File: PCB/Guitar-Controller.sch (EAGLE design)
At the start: 33 parts

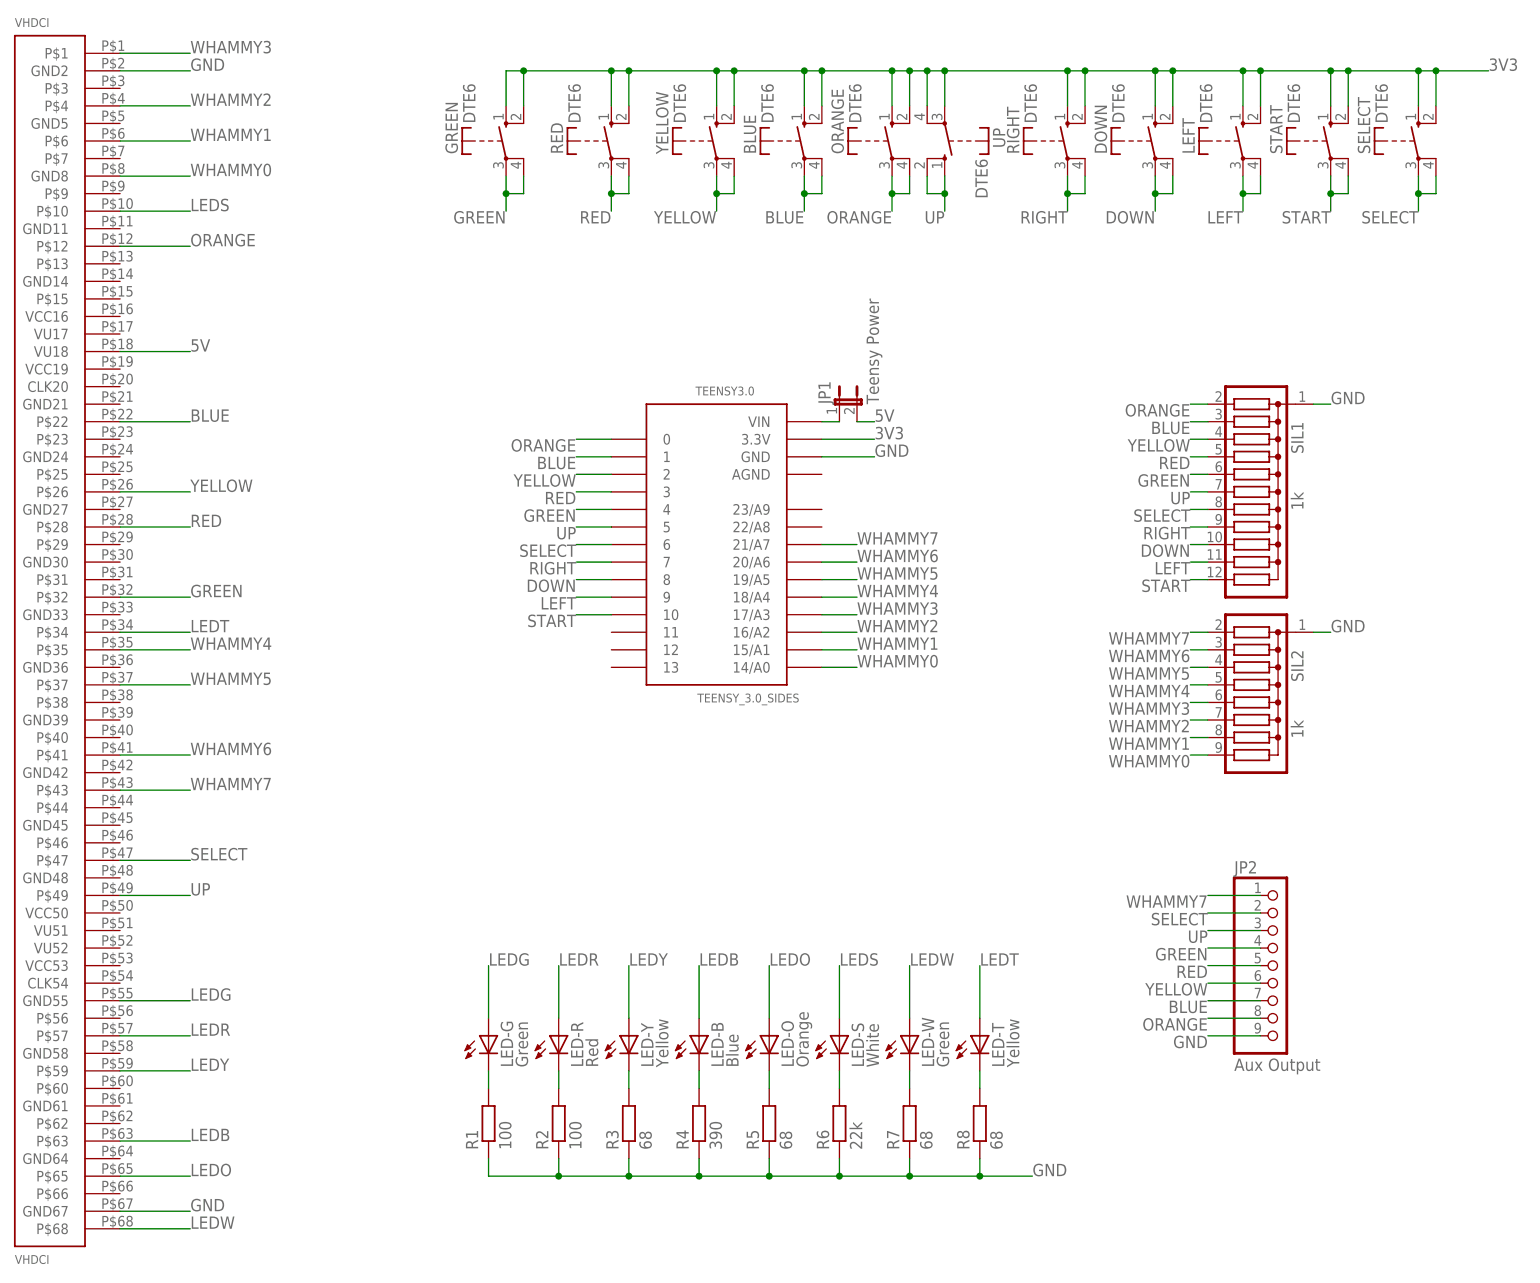
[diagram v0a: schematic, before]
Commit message: PCB: Changed all pin connections to use bottom layer
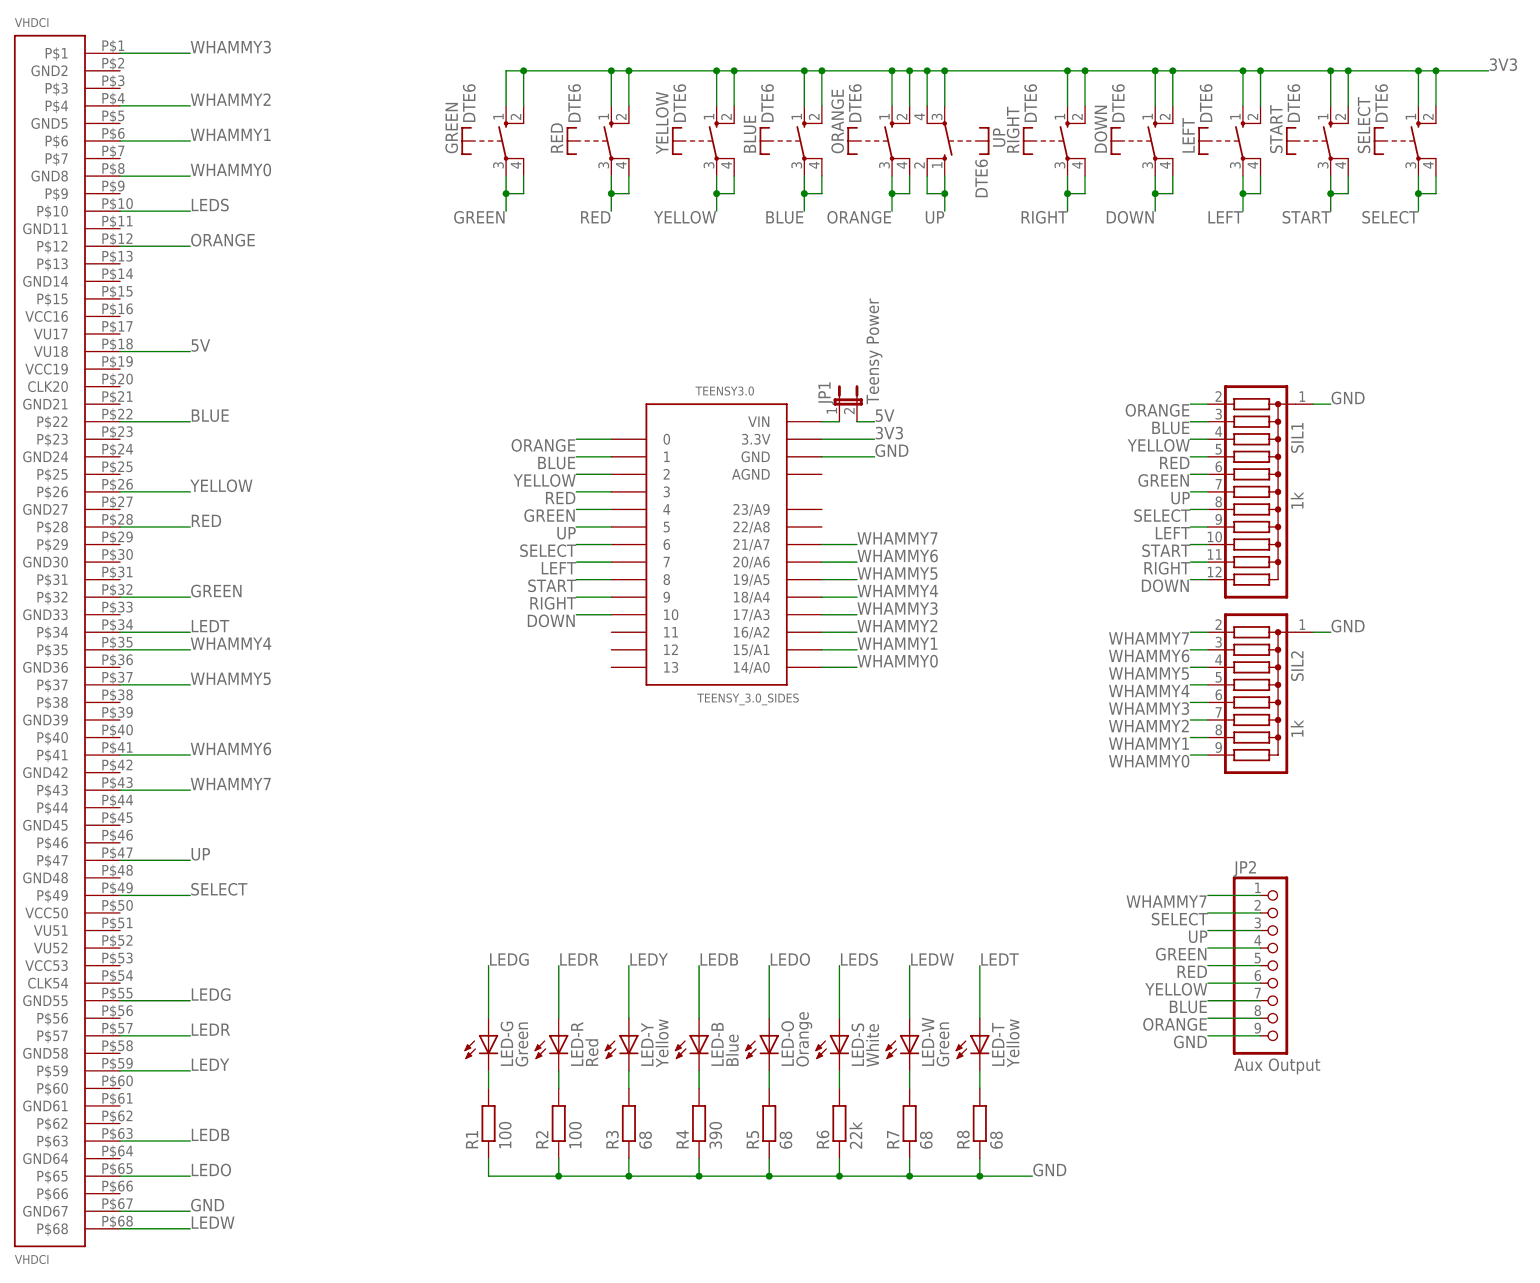
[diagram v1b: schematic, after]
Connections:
- net DOWN: now also SIL1.12, TEENSY3.0.10; no longer SIL1.10, TEENSY3.0.8
- net GND: no longer VHDCI.GND2
- net LEFT: now also SIL1.9, TEENSY3.0.7; no longer SIL1.11, TEENSY3.0.9
- net RIGHT: now also SIL1.11, TEENSY3.0.9; no longer SIL1.9, TEENSY3.0.7
- net SELECT: now also VHDCI.P$49; no longer VHDCI.P$47
- net START: now also SIL1.10, TEENSY3.0.8; no longer SIL1.12, TEENSY3.0.10
- net UP: now also VHDCI.P$47; no longer VHDCI.P$49
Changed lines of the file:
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@@
-</segment>
-<segment>
-<pinref part="VHDCI" gate="G$1" pin="GND2"/>
-<wire x1="-40.64" y1="127" x2="-30.48" y2="127" width="0.1524" layer="91"/>
-<label x="-30.48" y="127" size="1.778" layer="95"/>
 </segment>
 <segment>
@@
 </segment>
 <segment>
-<pinref part="VHDCI" gate="G$1" pin="P$49"/>
-<wire x1="-30.48" y1="7.62" x2="-40.64" y2="7.62" width="0.1524" layer="91"/>
-<label x="-30.48" y="7.62" size="1.778" layer="95"/>
+<pinref part="VHDCI" gate="G$1" pin="P$47"/>
+<wire x1="-30.48" y1="12.7" x2="-40.64" y2="12.7" width="0.1524" layer="91"/>
+<label x="-30.48" y="12.7" size="1.778" layer="95"/>
 </segment>
 </net>
@@
 </segment>
 <segment>
-<pinref part="SIL1" gate="A" pin="10"/>
-<wire x1="116.84" y1="58.42" x2="114.3" y2="58.42" width="0.1524" layer="91"/>
-<label x="114.3" y="58.42" size="1.778" layer="95" rot="R180"/>
-</segment>
-<segment>
-<pinref part="TEENSY3.0" gate="G$1" pin="8"/>
-<wire x1="30.48" y1="53.34" x2="25.4" y2="53.34" width="0.1524" layer="91"/>
-<label x="25.4" y="53.34" size="1.778" layer="95" rot="R180"/>
+<pinref part="TEENSY3.0" gate="G$1" pin="10"/>
+<wire x1="30.48" y1="48.26" x2="25.4" y2="48.26" width="0.1524" layer="91"/>
+<label x="25.4" y="48.26" size="1.778" layer="95" rot="R180"/>
+</segment>
+<segment>
+<pinref part="SIL1" gate="A" pin="12"/>
+<wire x1="116.84" y1="53.34" x2="114.3" y2="53.34" width="0.1524" layer="91"/>
+<label x="114.3" y="53.34" size="1.778" layer="95" rot="R180"/>
 </segment>
 </net>
@@
 </segment>
 <segment>
-<pinref part="SIL1" gate="A" pin="11"/>
-<wire x1="116.84" y1="55.88" x2="114.3" y2="55.88" width="0.1524" layer="91"/>
-<label x="114.3" y="55.88" size="1.778" layer="95" rot="R180"/>
-</segment>
-<segment>
-<pinref part="TEENSY3.0" gate="G$1" pin="9"/>
-<wire x1="30.48" y1="50.8" x2="25.4" y2="50.8" width="0.1524" layer="91"/>
-<label x="25.4" y="50.8" size="1.778" layer="95" rot="R180"/>
+<pinref part="TEENSY3.0" gate="G$1" pin="7"/>
+<wire x1="30.48" y1="55.88" x2="25.4" y2="55.88" width="0.1524" layer="91"/>
+<label x="25.4" y="55.88" size="1.778" layer="95" rot="R180"/>
+</segment>
+<segment>
+<pinref part="SIL1" gate="A" pin="9"/>
+<wire x1="116.84" y1="60.96" x2="114.3" y2="60.96" width="0.1524" layer="91"/>
+<label x="114.3" y="60.96" size="1.778" layer="95" rot="R180"/>
 </segment>
 </net>
@@
 </segment>
 <segment>
-<pinref part="SIL1" gate="A" pin="9"/>
-<wire x1="116.84" y1="60.96" x2="114.3" y2="60.96" width="0.1524" layer="91"/>
-<label x="114.3" y="60.96" size="1.778" layer="95" rot="R180"/>
-</segment>
-<segment>
-<pinref part="TEENSY3.0" gate="G$1" pin="7"/>
-<wire x1="30.48" y1="55.88" x2="25.4" y2="55.88" width="0.1524" layer="91"/>
-<label x="25.4" y="55.88" size="1.778" layer="95" rot="R180"/>
+<pinref part="TEENSY3.0" gate="G$1" pin="9"/>
+<wire x1="30.48" y1="50.8" x2="25.4" y2="50.8" width="0.1524" layer="91"/>
+<label x="25.4" y="50.8" size="1.778" layer="95" rot="R180"/>
+</segment>
+<segment>
+<pinref part="SIL1" gate="A" pin="11"/>
+<wire x1="116.84" y1="55.88" x2="114.3" y2="55.88" width="0.1524" layer="91"/>
+<label x="114.3" y="55.88" size="1.778" layer="95" rot="R180"/>
 </segment>
 </net>
@@
 </segment>
 <segment>
-<pinref part="SIL1" gate="A" pin="12"/>
-<wire x1="116.84" y1="53.34" x2="114.3" y2="53.34" width="0.1524" layer="91"/>
-<label x="114.3" y="53.34" size="1.778" layer="95" rot="R180"/>
-</segment>
-<segment>
-<pinref part="TEENSY3.0" gate="G$1" pin="10"/>
-<wire x1="30.48" y1="48.26" x2="25.4" y2="48.26" width="0.1524" layer="91"/>
-<label x="25.4" y="48.26" size="1.778" layer="95" rot="R180"/>
+<pinref part="TEENSY3.0" gate="G$1" pin="8"/>
+<wire x1="30.48" y1="53.34" x2="25.4" y2="53.34" width="0.1524" layer="91"/>
+<label x="25.4" y="53.34" size="1.778" layer="95" rot="R180"/>
+</segment>
+<segment>
+<pinref part="SIL1" gate="A" pin="10"/>
+<wire x1="116.84" y1="58.42" x2="114.3" y2="58.42" width="0.1524" layer="91"/>
+<label x="114.3" y="58.42" size="1.778" layer="95" rot="R180"/>
 </segment>
 </net>
@@
 </segment>
 <segment>
-<pinref part="VHDCI" gate="G$1" pin="P$47"/>
-<wire x1="-30.48" y1="12.7" x2="-40.64" y2="12.7" width="0.1524" layer="91"/>
-<label x="-30.48" y="12.7" size="1.778" layer="95"/>
-</segment>
-</net>
+<pinref part="VHDCI" gate="G$1" pin="P$49"/>
+<wire x1="-30.48" y1="7.62" x2="-40.64" y2="7.62" width="0.1524" layer="91"/>
+<label x="-30.48" y="7.62" size="1.778" layer="95"/>
+</segment>
+</net>

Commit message: PCB: Fixed errors on VHDC connector and changed SILs SIL change is to work with what is available in department
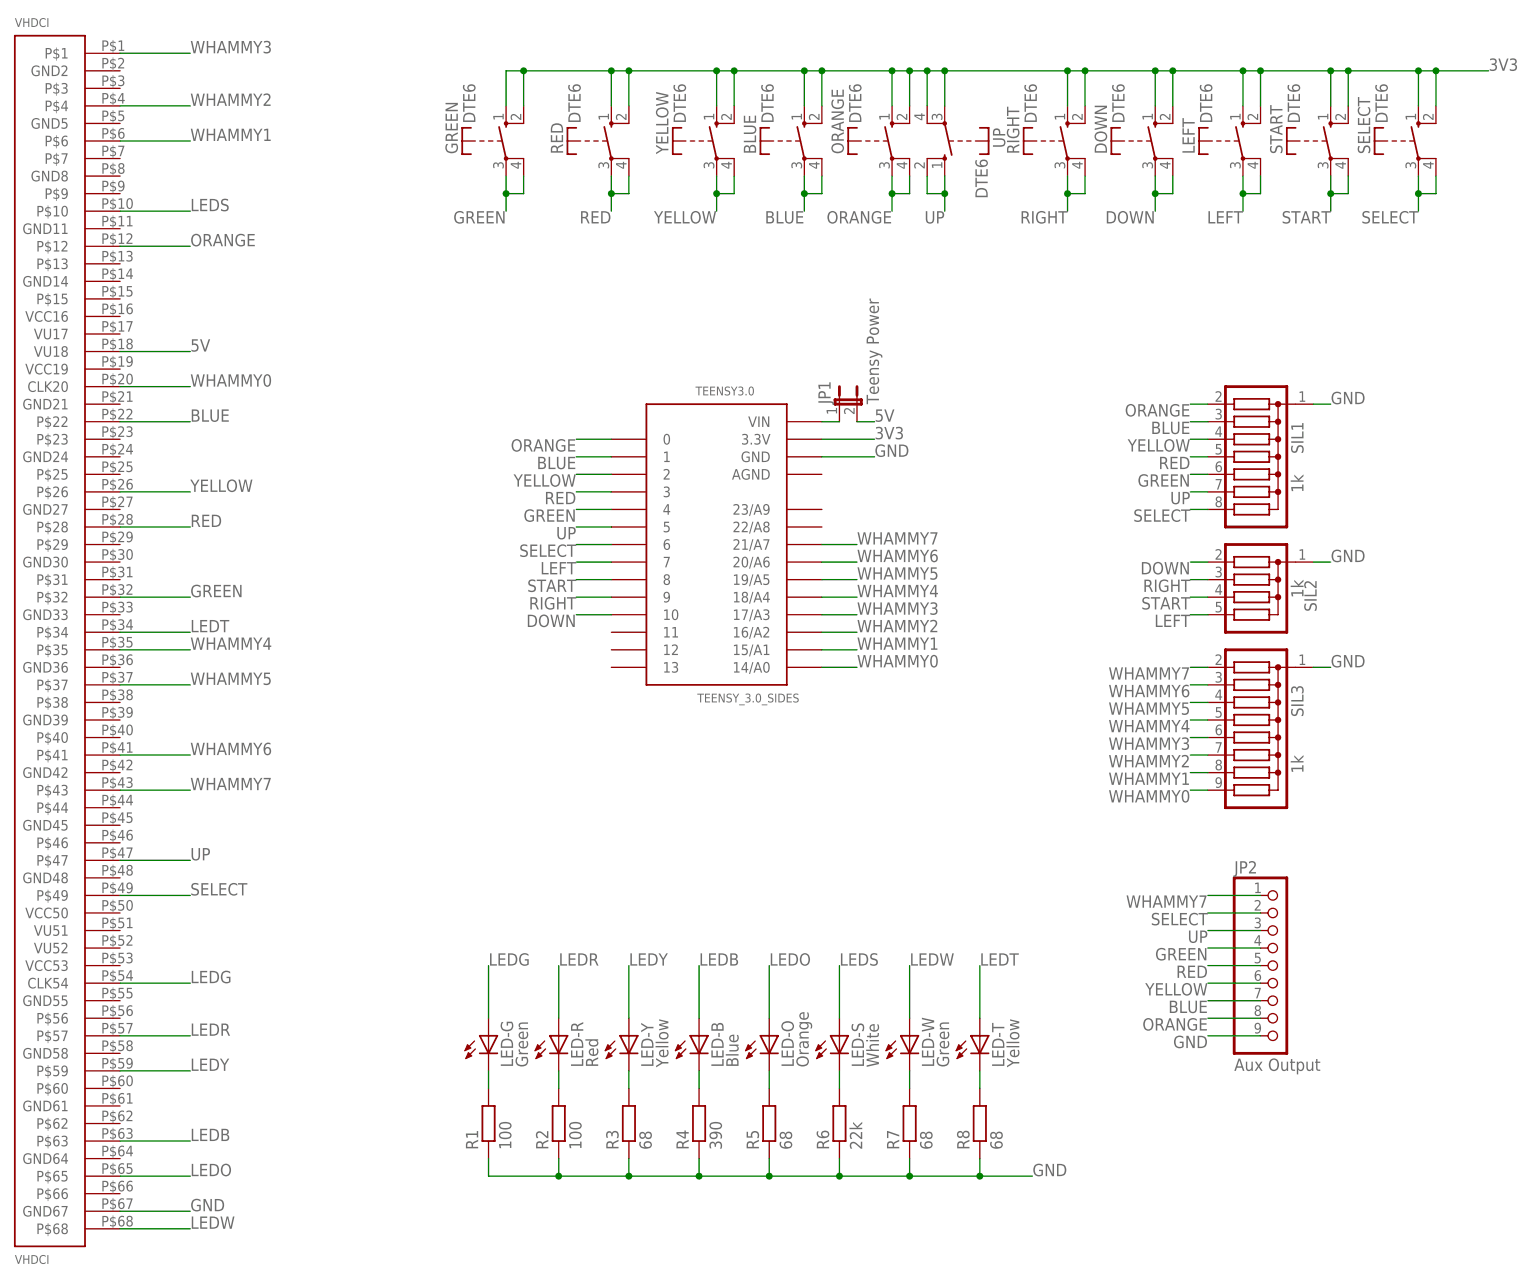
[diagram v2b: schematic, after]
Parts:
- added SIL3: 1k, resistor-sil:G08R
- SIL1: device resistor-sil:G11R -> resistor-sil:G07R
- SIL2: device resistor-sil:G08R -> resistor-sil:G04R; OC_FARNELL (none) -> unknown; OC_NEWARK (none) -> unknown
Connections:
- net DOWN: now also SIL2.2; no longer SIL1.12
- net GND: now also SIL3.1
- net LEDG: now also VHDCI.CLK54; no longer VHDCI.GND55
- net LEFT: now also SIL2.5; no longer SIL1.9
- net RIGHT: now also SIL2.3; no longer SIL1.11
- net START: now also SIL2.4; no longer SIL1.10
- net WHAMMY0: now also SIL3.9, VHDCI.CLK20; no longer SIL2.9, VHDCI.GND8
- net WHAMMY1: now also SIL3.8; no longer SIL2.8
- net WHAMMY2: now also SIL3.7; no longer SIL2.7
- net WHAMMY3: now also SIL3.6; no longer SIL2.6
- net WHAMMY4: now also SIL3.5; no longer SIL2.5
- net WHAMMY5: now also SIL3.4; no longer SIL2.4
- net WHAMMY6: now also SIL3.3; no longer SIL2.3
- net WHAMMY7: now also SIL3.2; no longer SIL2.2
